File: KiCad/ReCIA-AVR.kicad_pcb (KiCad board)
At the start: 4 copper layers, 17.4 x 51.4 mm, 20 parts, among them U1 AVR128DA64-I_MR, U2 74AHCT1G17, U3 TLC2932AIPWR, U5 8520_DIP

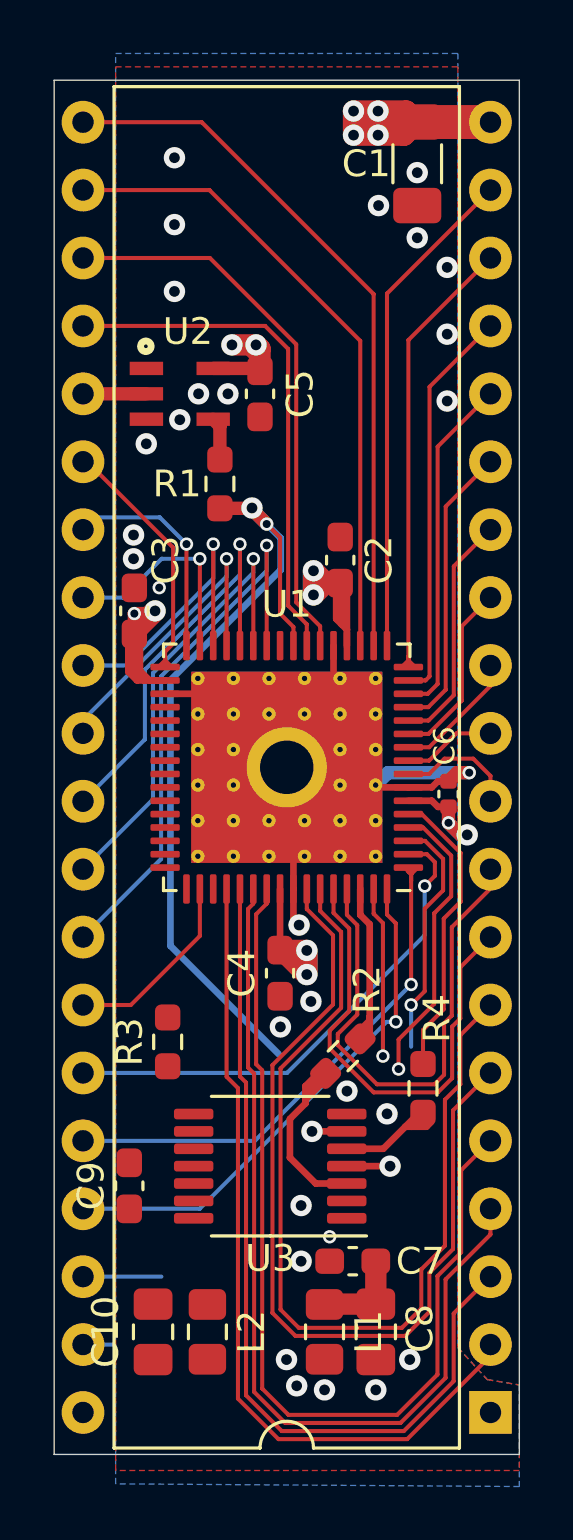
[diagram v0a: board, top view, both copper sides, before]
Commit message: Add pull-up resistor on SELECT-line and more placement and routing fixes
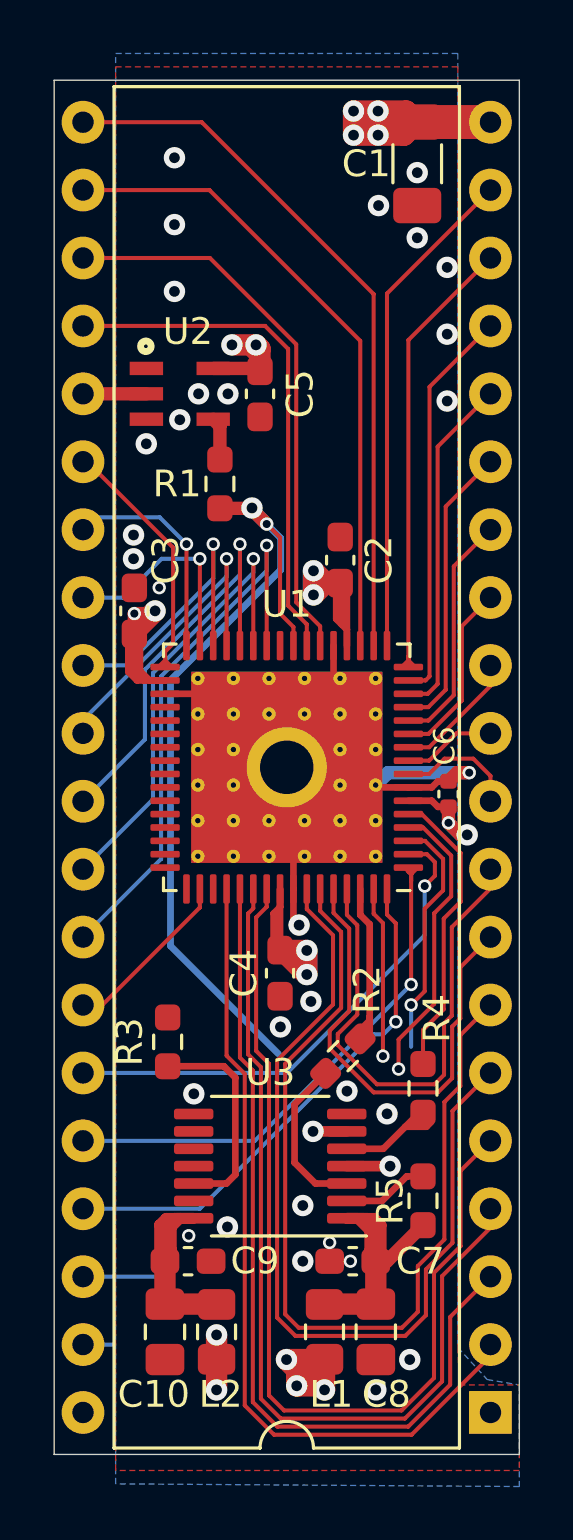
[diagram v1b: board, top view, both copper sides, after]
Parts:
- added R5: 33, Resistor_SMD:R_0603_1608Metric_Pad0.98x0.95mm_HandSolder, F.Cu at (137.1, 99.2)
- moved C9 3.57 mm to (128.3, 101.5), turned to 0 degrees
- moved C10 0.44 mm to (127.4, 104.1)
- moved L2 0.34 mm to (129.4, 104.1)
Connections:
- U3 pad 2: Net-(U3-Pad2) -> /SELECT
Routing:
- net VCC: track 49.8 -> 60.7 mm, vias 17 -> 19
- net /VCO_VDD: track 0.00 -> 10.7 mm
- net /LOGIC_VDD: track 4.04 -> 14.2 mm
- net /VCO_IN: track 0.00 -> 8.03 mm
- net /SELECT: track 0.00 -> 3.23 mm
- net /VCO_OUT: track 8.40 -> 6.40 mm
- net RESET: track 7.20 -> 6.57 mm
- net GND: vias 27 -> 31

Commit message: Add 3.3k resistor and 0.22uF cap for the RBIAS-pin on the PLL
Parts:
- removed the C10 at (127.4, 104.1)
- added C11: 0.22uF, Capacitor_SMD:C_0603_1608Metric_Pad1.08x0.95mm_HandSolder, F.Cu at (126.2, 99.5)
- added C2: 10uF, Capacitor_SMD:C_0805_2012Metric_Pad1.18x1.45mm_HandSolder, F.Cu at (127.4, 104.1)
- added R6: 3k3, Resistor_SMD:R_0603_1608Metric_Pad0.98x0.95mm_HandSolder, F.Cu at (128.3, 107.7)
- renumbered C2 to C10, C8 to C3, C3 to C8
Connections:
- U3 pad 13: Net-(U3-Pad13) -> /RBIAS
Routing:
- net /RBIAS: track 0.00 -> 11.0 mm
- net /VCO_VDD: track 10.7 -> 18.1 mm
- net VCC: track 60.7 -> 62.4 mm, vias 19 -> 20
- net GND: vias 31 -> 34

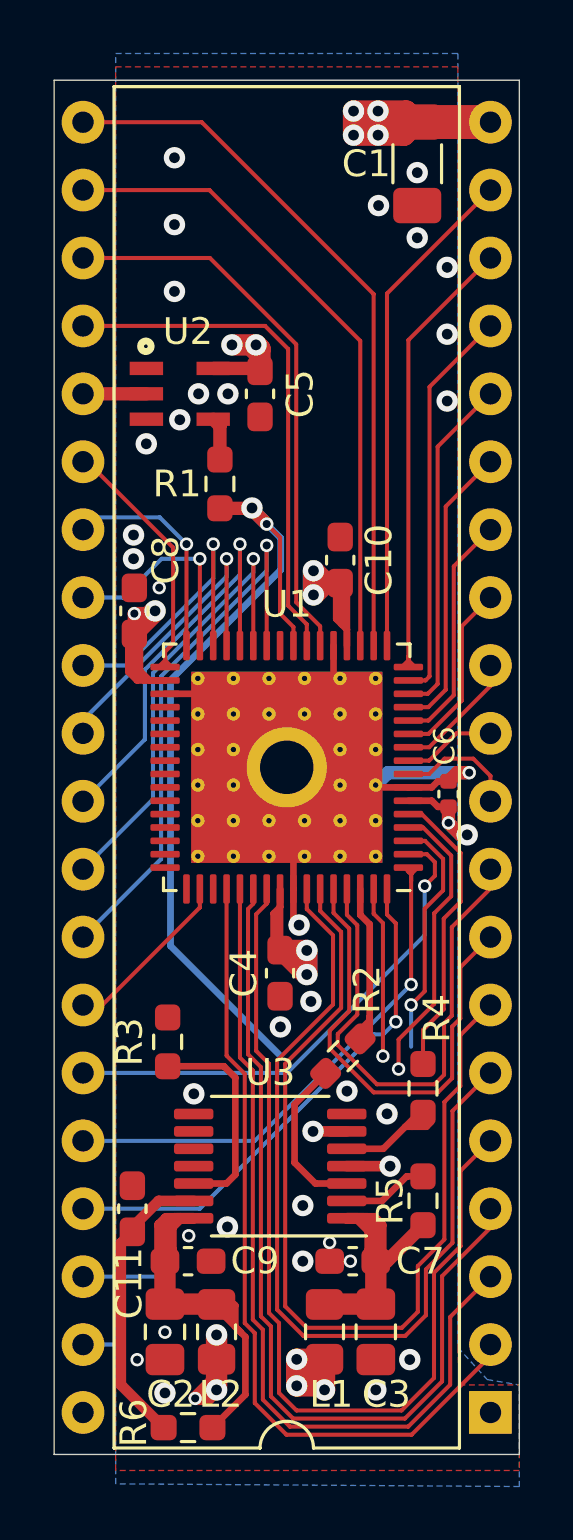
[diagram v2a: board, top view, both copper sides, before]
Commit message: Add cap for the VCO_IN-pin on the PLL
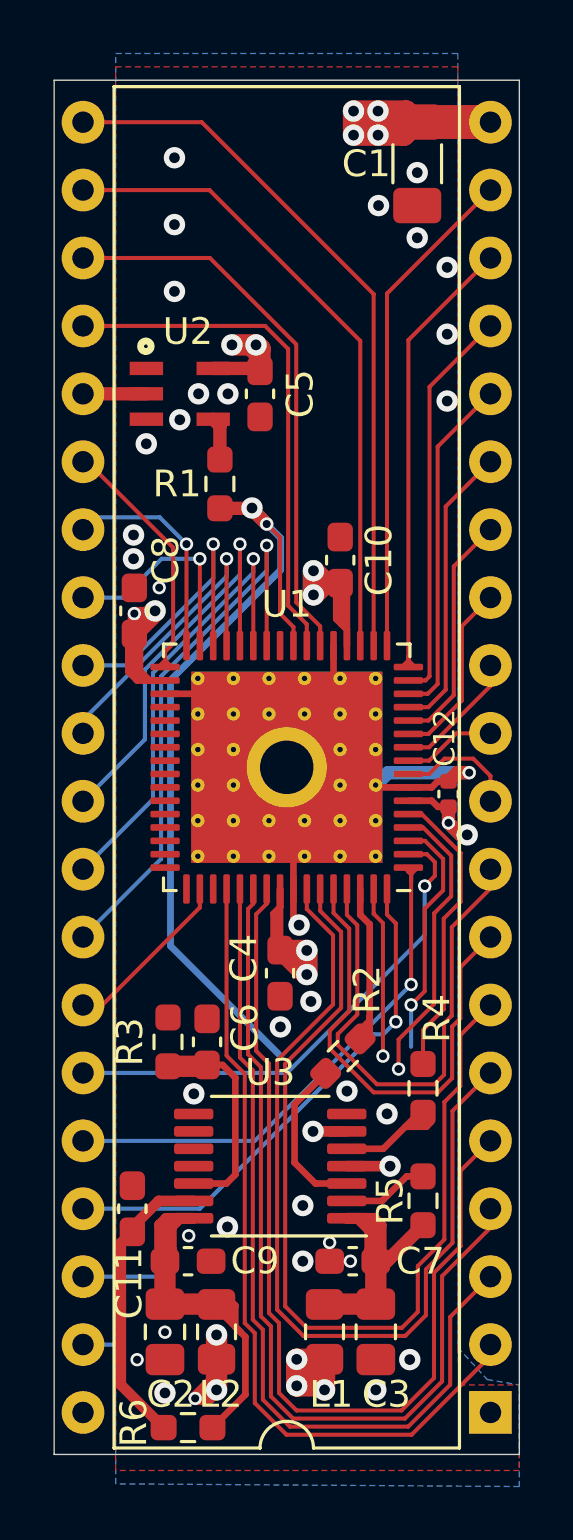
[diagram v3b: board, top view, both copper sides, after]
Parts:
- added C6: 0.1uF, Capacitor_SMD:C_0603_1608Metric_Pad1.08x0.95mm_HandSolder, F.Cu at (129.0, 93.3)
- renumbered C6 to C12

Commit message: Change from 0805 to 1206 size on C2 and C3
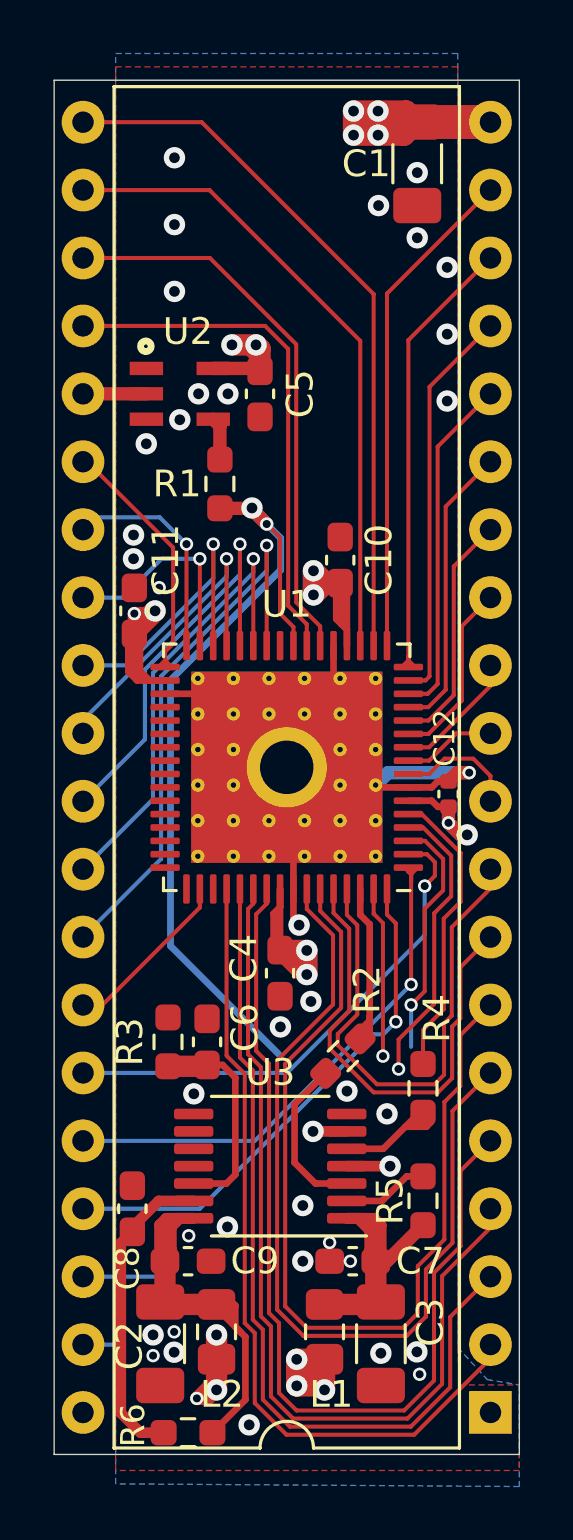
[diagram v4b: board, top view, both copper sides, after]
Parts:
- C2, C3: footprint Capacitor_SMD:C_0805_2012Metric_Pad1.18x1.45mm_HandSolder -> Capacitor_SMD:C_1206_3216Metric_Pad1.33x1.80mm_HandSolder
- moved C3 0.48 mm to (135.5, 104.6)
- moved C2 0.48 mm to (127.3, 104.6)
- moved R6 0.19 mm to (128.3, 107.9)
- renumbered C8 to C11, C11 to C8
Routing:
- net /RBIAS: track 11.0 -> 11.7 mm
- net /VCO_VDD: track 18.1 -> 18.6 mm
- net GND: vias 34 -> 37

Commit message: Add resistor and cap on VCO_IN line
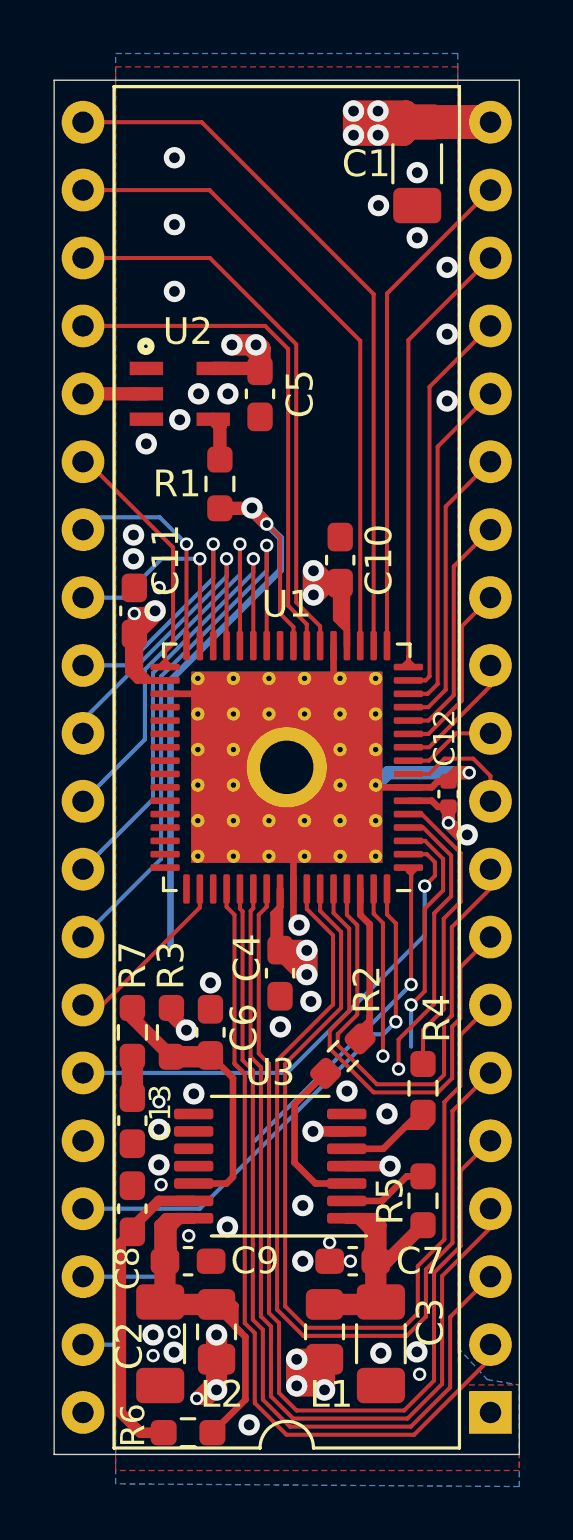
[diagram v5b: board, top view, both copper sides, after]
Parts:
- added C13: 0.1uF, Capacitor_SMD:C_0603_1608Metric_Pad1.08x0.95mm_HandSolder, F.Cu at (126.2, 96.2)
- added R7: 33, Resistor_SMD:R_0603_1608Metric_Pad0.98x0.95mm_HandSolder, F.Cu at (126.2, 92.9)
- moved C6 0.38 mm to (129.1, 92.9)
- moved R3 0.38 mm to (127.7, 92.9)
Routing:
- net A2: track 20.9 -> 14.5 mm
- net E-CLK: track 34.9 -> 29.1 mm
- net /VCO_IN: track 8.06 -> 10.4 mm
- net /PFD_OUT: track 7.10 -> 8.63 mm, vias 1 -> 2
- net Net-(C13-Pad2): track 0.00 -> 1.53 mm
- net PA0: track 30.7 -> 31.2 mm
- net GND: vias 37 -> 42

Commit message: Fixed caps and resistor references enumeration, more routing and small fixes positioning vias
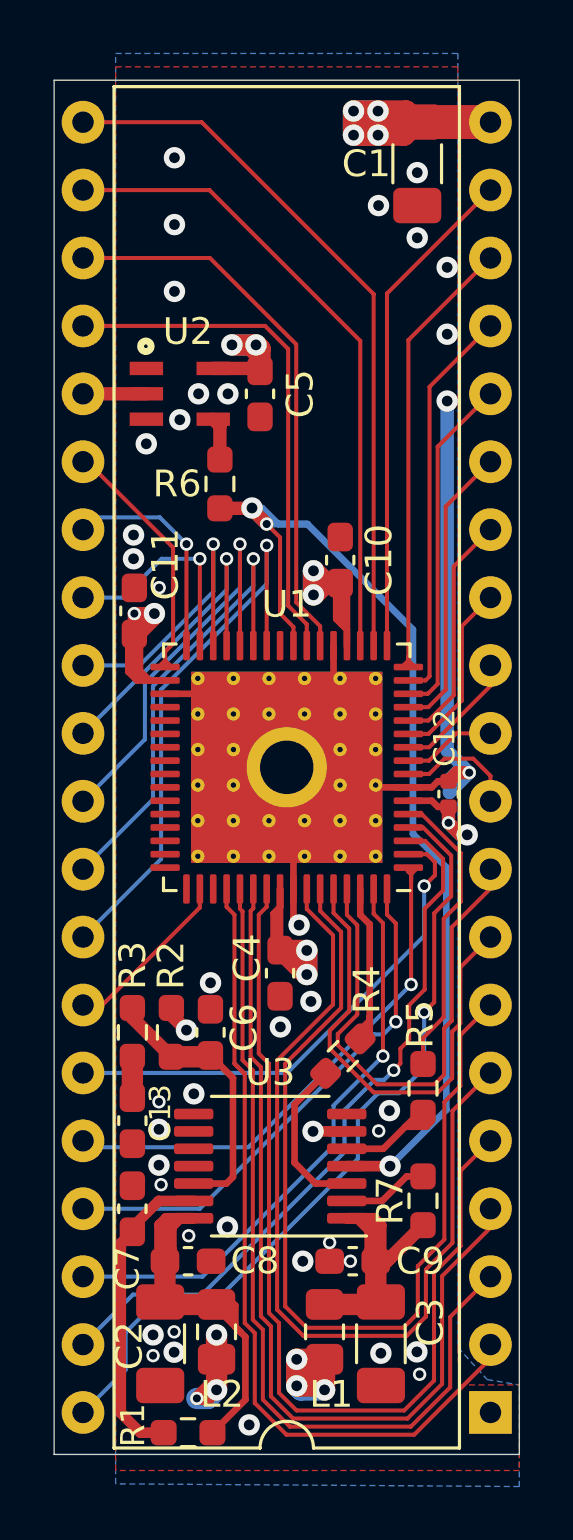
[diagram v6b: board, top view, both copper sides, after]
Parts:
- R7: renamed from R5; value 33 -> 10k
- renumbered C8 to C7, C9 to C8, C7 to C9, R6 to R1, R3 to R2, R7 to R3, R2 to R4, R4 to R5, R1 to R6
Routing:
- net CNT: track 11.4 -> 30.9 mm
- net SP: track 10.2 -> 27.0 mm
- net E-CLK: track 29.1 -> 42.3 mm
- net GND: track 29.0 -> 42.0 mm, vias 42 -> 41
- net A0: track 9.33 -> 21.9 mm
- net VCC: track 62.4 -> 72.6 mm
- net A2: track 14.5 -> 21.1 mm

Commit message: corrected C8,C9 to 0.1uF
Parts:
- C8, C9: value 0.01uF -> 0.1uF
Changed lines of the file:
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@@
       (effects (font (size 1 1) (thickness 0.15)))
     )
-    (fp_text value 0.01uF (at 0 1.43) (layer F.Fab) hide
+    (fp_text value 0.1uF (at 0 1.43) (layer F.Fab) hide
       (effects (font (size 1 1) (thickness 0.15)))
     )
@@
       (effects (font (size 1 1) (thickness 0.15)))
     )
-    (fp_text value 0.01uF (at 0 1.43) (layer F.Fab) hide
+    (fp_text value 0.1uF (at 0 1.43) (layer F.Fab) hide
       (effects (font (size 1 1) (thickness 0.15)))
     )

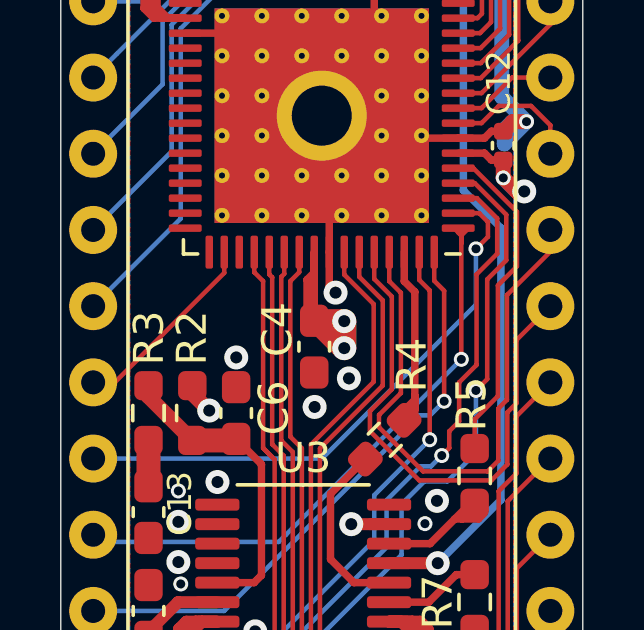
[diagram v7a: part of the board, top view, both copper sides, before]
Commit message: Add UPDI pin-header
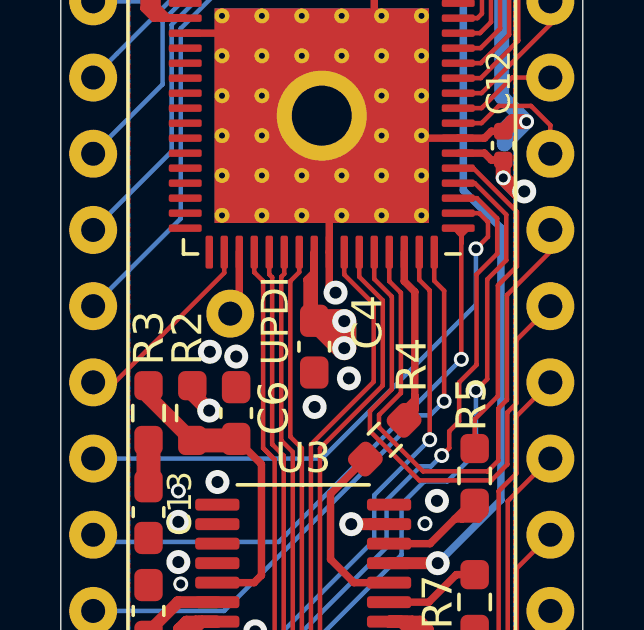
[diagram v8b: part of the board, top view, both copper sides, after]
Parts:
- added UPDI: Conn_01x01, Connector_PinHeader_2.54mm:PinHeader_1x01_P2.54mm_Vertical, F.Cu at (128.9, 89.6)
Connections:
- U1 pad 51: UDPI -> /UPDI
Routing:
- net /UPDI: track 0.00 -> 2.17 mm
- net GND: vias 41 -> 42
